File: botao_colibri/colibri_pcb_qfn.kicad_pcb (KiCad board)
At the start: 4 copper layers, 15.6 x 38.3 mm, 43 parts, among them IC1 VCNL36826M, J1 USB4970-00-A_REVA, J2 TC2030, SW1 B3F-3122, U1 ME54BS12, U3 LSM6DSV16XTR, U4 NPM1300-QEAA-R7

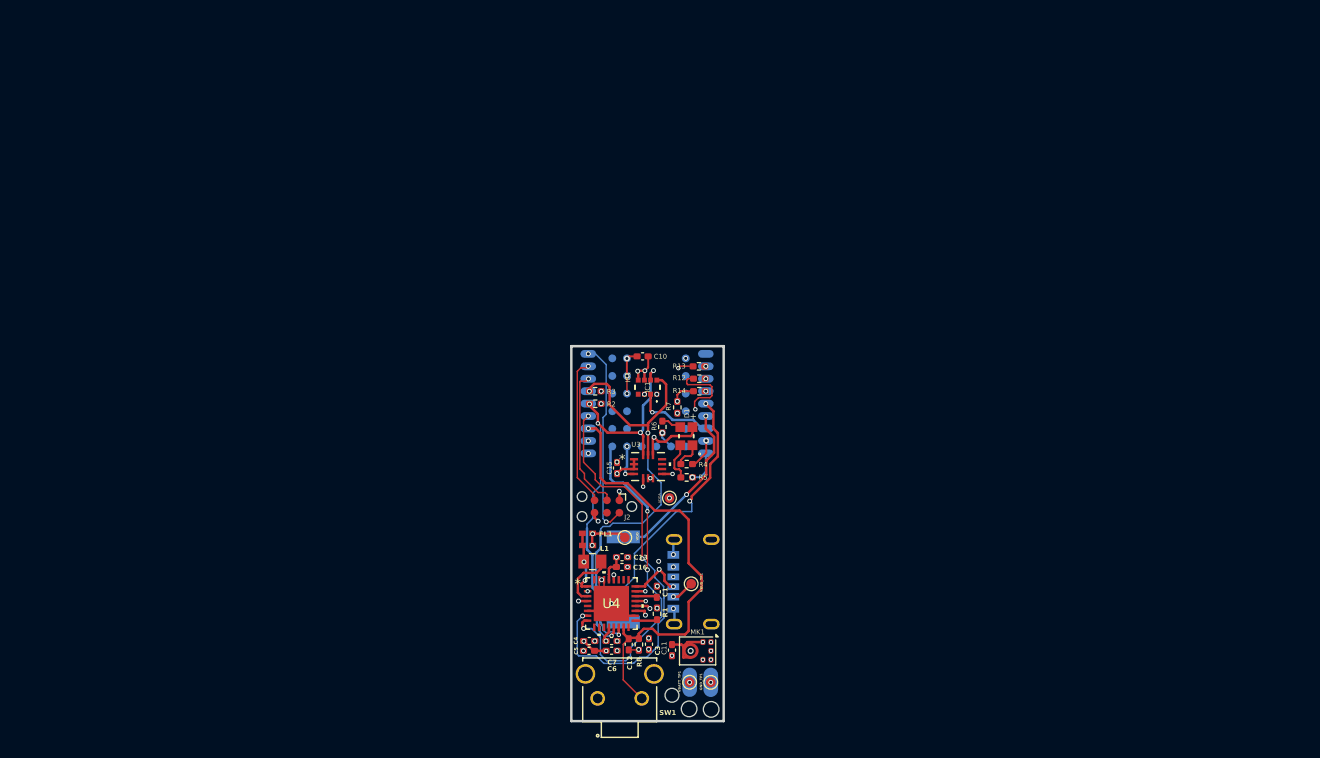
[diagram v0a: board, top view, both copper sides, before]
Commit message: chore: Update PCB/schematic edits and project files
Marks hole positions on the board, syncs KiCad project/prl files after
enabling the colibri-v4 library, and adds the botao_colibri KiCad
project files plus recent backup snapshots.

Co-Authored-By: Claude Sonnet 5 <noreply@anthropic.com>
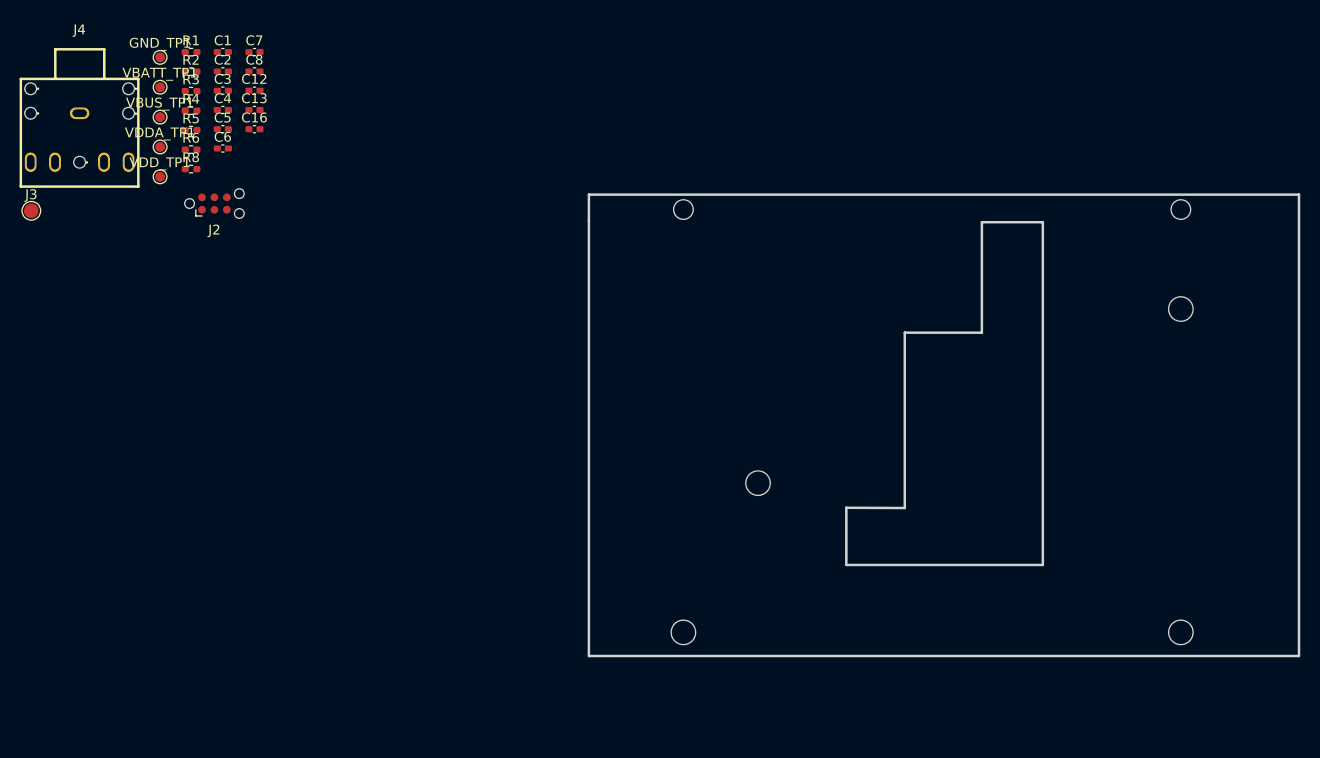
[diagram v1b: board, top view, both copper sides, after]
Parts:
- removed ?: , Pad_ie19
- removed ?: , Pad_ie20
- removed C10, C11: C_Small, Capacitor_SMD:C_0402_1005Metric_Pad0.74x0.62mm_HandSolder
- removed C15: 100nF, Capacitor_SMD:C_0402_1005Metric_Pad0.74x0.62mm_HandSolder
- removed D1: WL-SFCD_0805, colibri-v4:WL-SFCD_0805
- removed FL1 (x2): BLM15AG121SN1D, colibri-v4:IND_BLM15_0402_MUR
- removed IC1: VCNL36826M, colibri-v4:VCNL36826M
- removed J1: USB4970-00-A_REVA, colibri-v4:GCT_USB4970-00-A_REVA
- removed L1: 2.2µH, colibri-v4:LQM21PN2R2MGRD
- removed LS1: PKMCS0909E4000-R1, colibri-v4:SPKR_PKMCS0909E4000-R1
- removed MK1: SPH0645LM4H, Sensor_Audio:Knowles_SPH0645LM4H-6_3.5x2.65mm
- removed R12, R13, R14: 51R, Resistor_SMD:R_0402_1005Metric_Pad0.72x0.64mm_HandSolder
- removed R7: 100kR, Resistor_SMD:R_0402_1005Metric_Pad0.72x0.64mm_HandSolder
- removed SW1: B3F-3122, colibri-v4:B3F-3122
- removed U1: ME54BS12, colibri-v4:ME54BS12_V1.0
- removed U3: LSM6DSV16XTR, colibri-v4:LGA-14L_STM
- removed U4: NPM1300-QEAA-R7, colibri-v4:NPM1300_QFN32_5X5_NOR
- removed VDD, VDDA: TestPoint, TestPoint:TestPoint_Pad_D1.0mm
- added C2: 10µF, Capacitor_SMD:C_0402_1005Metric_Pad0.74x0.62mm_HandSolder, F.Cu at (86.6, 59.9)
- added C8: C_Small, Capacitor_SMD:C_0402_1005Metric_Pad0.74x0.62mm_HandSolder, F.Cu at (89.9, 59.9)
- added H1: NPTH, NPTH, F.Cu at (184.5, 84.2)
- added H2: NPTH, NPTH, F.Cu at (133.7, 117.2)
- added H3: NPTH, NPTH, F.Cu at (184.5, 117.2)
- added H4: NPTH, NPTH, F.Cu at (141.3, 101.9)
- added H5: NPTH, NPTH, F.Cu at (133.7, 74.0)
- added H6: NPTH, NPTH, F.Cu at (184.5, 74.0)
- added J3: Conn_01x02, TestPoint:TestPoint_Pad_D1.5mm, F.Cu at (67.1, 74.1)
- added J4: PJ-307C, botao_colibri:AUDIO-TH_PJ307C, F.Cu at (72.0, 66.7)
- added VDDA_TP1: TestPoint, TestPoint:TestPoint_Pad_D1.0mm, F.Cu at (80.2, 67.6)
- added VDD_TP1: TestPoint, TestPoint:TestPoint_Pad_D1.0mm, F.Cu at (80.2, 70.7)
- R2, R3: value R_Small -> 4.7kR
- moved GND_TP1 85.1 mm to (80.2, 58.5)
- moved VBATT_TP1 81.3 mm to (80.2, 61.5)
- moved R1 74.5 mm to (83.4, 57.9), turned to 0 degrees
- moved VBUS_TP1 72.2 mm to (80.2, 64.6)
- moved C3 71.3 mm to (86.6, 61.9), turned to 0 degrees
- moved C1 70.7 mm to (86.6, 57.9), turned to 0 degrees
- moved C7 70.3 mm to (89.9, 57.9)
- moved C12 68.2 mm to (89.9, 61.9), turned to 0 degrees
- moved R8 66.7 mm to (83.4, 69.9), turned to 0 degrees
- moved C4 65.9 mm to (86.6, 63.8)
- moved C5 65.1 mm to (86.6, 65.8), turned to 0 degrees
- moved C6 64.9 mm to (86.6, 67.8)
- moved R4 62.2 mm to (83.4, 63.9), turned to 0 degrees
- moved R5 61.8 mm to (83.4, 65.9)
- moved C13 59.1 mm to (89.9, 63.8)
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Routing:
- net VDD: track 83.4 -> 0.00 mm, vias 12 -> 0
- net I2C_SCL: track 47.1 -> 0.00 mm, vias 3 -> 0
- net BTN_PWR: track 44.8 -> 0.00 mm, vias 1 -> 0
- net NPM1300_INT: track 42.7 -> 0.00 mm, vias 3 -> 0
- net I2C_SDA: track 42.6 -> 0.00 mm, vias 5 -> 0
- net Net-(MK1-DATA): track 40.7 -> 0.00 mm, vias 2 -> 0
- net VDDA: track 38.0 -> 0.00 mm, vias 6 -> 0
- net Net-(MK1-BCLK): track 36.9 -> 0.00 mm, vias 2 -> 0
- net Net-(MK1-WS): track 36.6 -> 0.00 mm, vias 2 -> 0
- net NPM1300_EN: track 34.2 -> 0.00 mm, vias 3 -> 0
- net GND: track 30.7 -> 0.00 mm, vias 28 -> 0
- net BUZZER_PWM_N: track 27.9 -> 0.00 mm, vias 2 -> 0
- net PVDD: track 27.0 -> 0.00 mm, vias 5 -> 0
- net NRESET: track 20.3 -> 0.00 mm, vias 2 -> 0
- net BUZZER_PWM_P: track 17.8 -> 0.00 mm, vias 2 -> 0
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- removed copper zone on In1.Cu, net GND
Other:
- board size 15.6 x 38.3 mm -> 72.5 x 47.1 mm
- copper layers 4 -> 2
- board text removed: "+"
- board text removed: "-"
